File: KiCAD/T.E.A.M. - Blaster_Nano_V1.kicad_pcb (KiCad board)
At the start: 2 copper layers, 100.2 x 60 mm, 47 parts, among them J1 USB_C_Receptacle_USB2.0_14P, J2 Akku, J3 LED, J4 Taster, J5 Speaker, J6 Conn_02x03_Counter_Clockwise, Q1 FS8205A, U1 TP4056-42-ESOP8, U2 DW01A, U3 MT3608, U4 ATMEGA328P-AU, U5 CH340G, U6 DFR0299, Y1 Crystal_GND34, Y2 Crystal_GND34

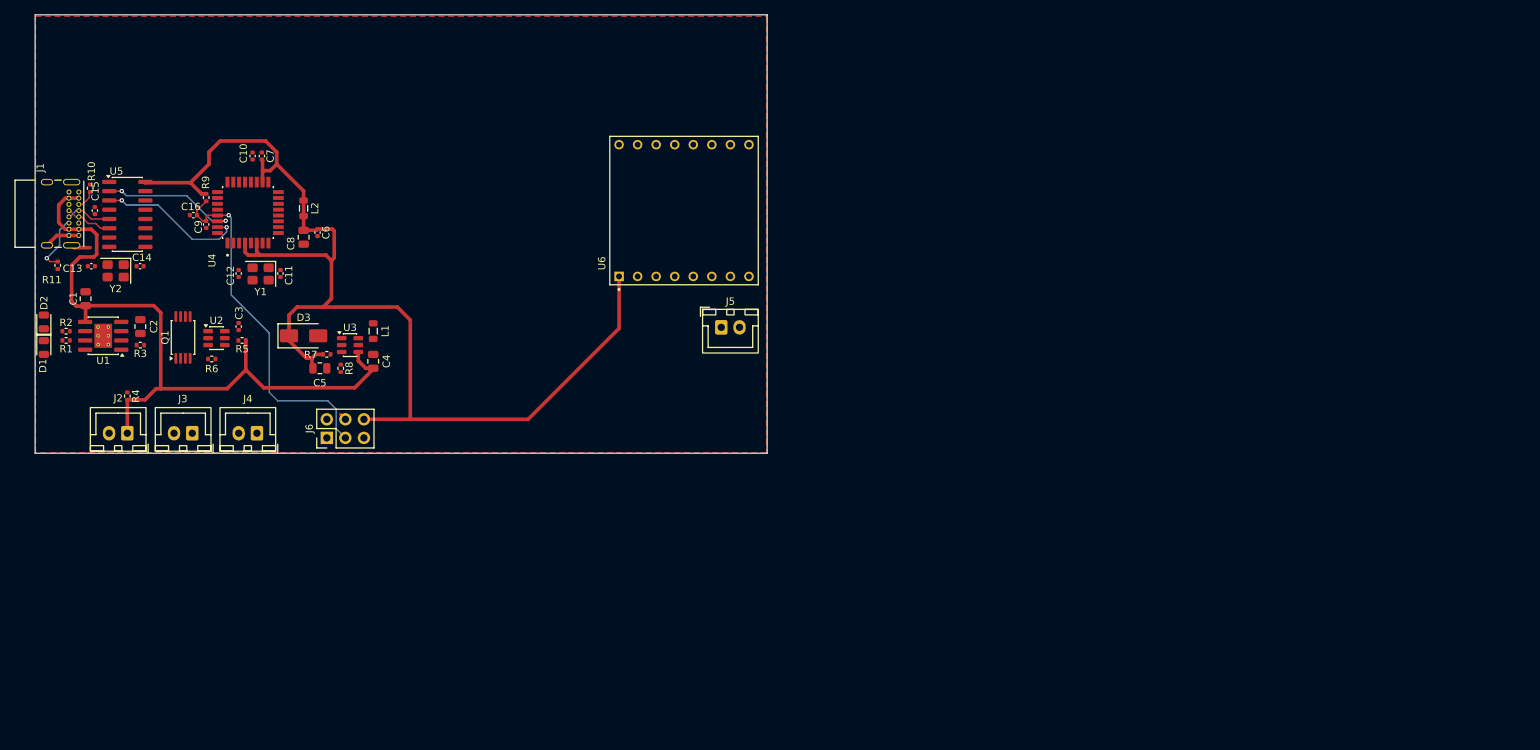
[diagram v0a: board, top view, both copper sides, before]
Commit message: Schaltplan finalisiert: alle Sektoren abgeschlossen
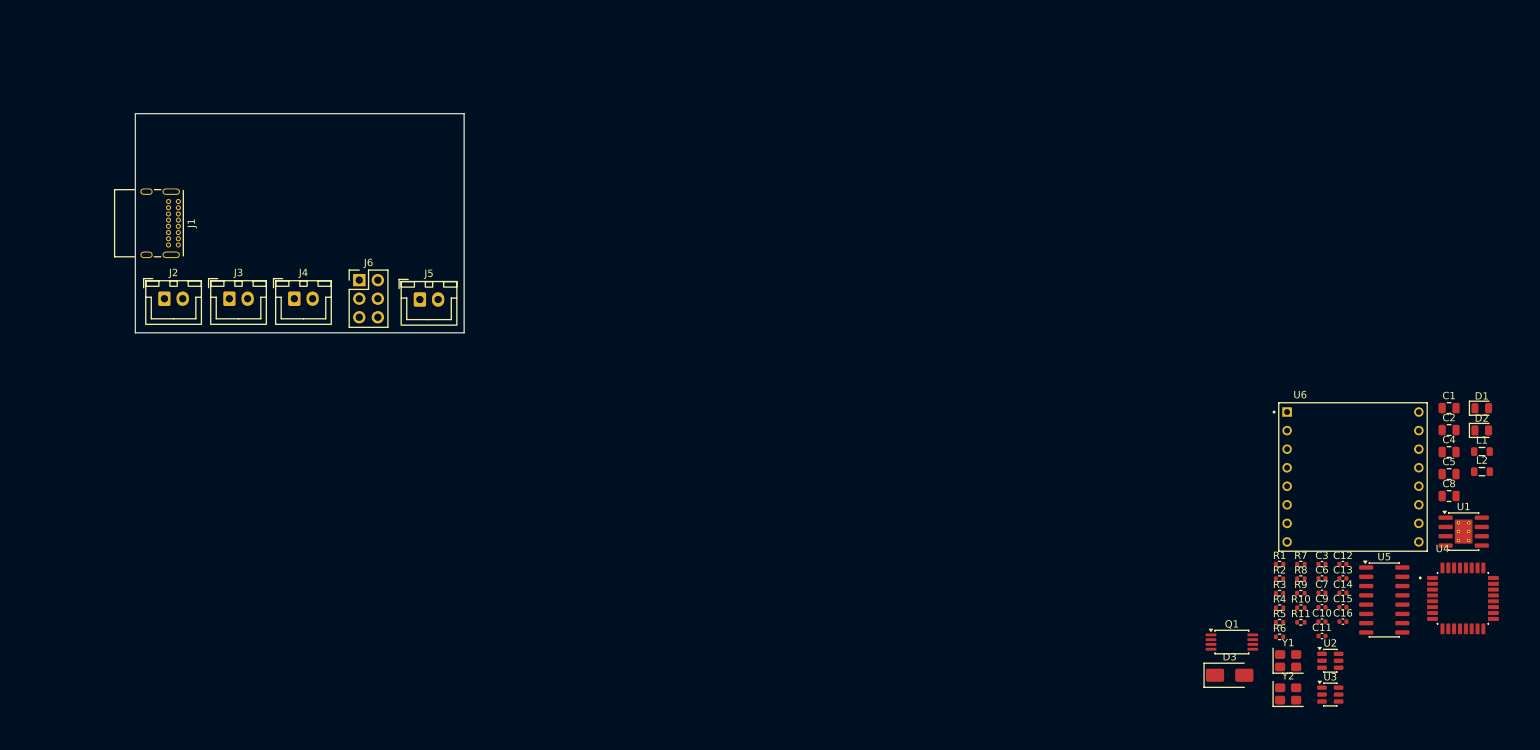
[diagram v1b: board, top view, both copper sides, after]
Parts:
- D1: value LED rot -> LED
- D2: value LED blau -> LED
- J6: value Conn_02x03_Counter_Clockwise -> ISP Bootloader
- moved D2 197.4 mm to (274.3, 118.4), turned to 0 degrees
- moved D1 197.0 mm to (274.3, 115.3), turned to 0 degrees
- moved U1 188.1 mm to (271.8, 132.2), turned to 0 degrees
- moved C1 187.2 mm to (269.8, 115.3), turned to 0 degrees
- moved U5 180.0 mm to (261.0, 141.6)
- moved C2 179.7 mm to (269.8, 118.3), turned to 0 degrees
- moved C15 179.3 mm to (255.3, 142.6), turned to 0 degrees
- moved R11 177.0 mm to (249.5, 144.6), turned to 0 degrees
- moved C13 176.6 mm to (255.3, 138.6)
- moved R10 175.4 mm to (249.5, 142.6), turned to 0 degrees
- moved U4 174.5 mm to (271.7, 141.3), turned to 0 degrees
- moved Y2 170.6 mm to (247.8, 154.4), turned to 0 degrees
- moved C14 170.6 mm to (255.3, 140.6), turned to 0 degrees
- moved R2 169.5 mm to (246.6, 138.7)
- moved R1 168.9 mm to (246.6, 136.7), turned to 0 degrees
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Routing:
- net VCC: track 162.8 -> 0.00 mm
- net VBATT: track 98.5 -> 0.00 mm
- net /RESET: track 48.9 -> 0.00 mm, vias 1 -> 0
- net /MCU_TX: track 20.6 -> 0.00 mm, vias 2 -> 0
- net /MCU_RX: track 18.8 -> 0.00 mm, vias 2 -> 0
- net GND: track 8.49 -> 0.00 mm
- net Net-(J1-CC2): track 8.25 -> 0.00 mm, vias 1 -> 0
- net /USB_DM: track 6.52 -> 0.00 mm
- net /USB_DP: track 6.34 -> 0.00 mm
- net Net-(J1-CC1): track 2.64 -> 0.00 mm
- removed copper zone on F.Cu, net GND
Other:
- board size 100.2 x 60 mm -> 45 x 30 mm

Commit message: Sektor 1: Placement und Routing abgeschlossen
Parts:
- removed C9: C, Capacitor_SMD:C_0402_1005Metric
- C1, C2, C8: value C -> 10 µF
- C10, C15, C16, C3, C6, C7: value C -> 100 nF
- C11, C12, C13, C14: value C -> 22 pF
- C4: value C -> 22µF
- C5: value C -> 22 µF
- D1: value LED -> LED rot
- D2: value LED -> LED blau
- J6: value ISP Bootloader -> Conn_02x03_Counter_Clockwise
- L1, L2: value L_Small -> 10 µH
- R1, R2: value R -> 1kΩ
- R10, R11: value R -> 5.1 kΩ
- R3: value R -> 2.4 kΩ
- R4: value R -> 470 Ω
- R5: value R -> 100 Ω
- R6: value R -> 1 kΩ
- R7: value R -> 180 kΩ
- R8: value R -> 27 kΩ
- R9: value R -> 10 kΩ
- Y1: value Crystal_GND34 -> 16 MHz
- Y2: value Crystal_GND34 -> 12 MHz
- moved U1 174.9 mm to (103.9, 83.2)
- moved C2 173.0 mm to (99.7, 87.0)
- moved D2 167.9 mm to (109.8, 84.5)
- moved D1 167.8 mm to (109.8, 81.9)
- moved C1 166.2 mm to (106.0, 87.0)
- moved R10 163.9 mm to (97.8, 80.6), turned to 90 degrees
- moved R11 162.3 mm to (99.1, 83.8)
- moved U2 161.9 mm to (102.3, 92.2), turned to 90 degrees
- moved R4 159.0 mm to (98.4, 85.1), turned to 180 degrees
- moved R3 158.3 mm to (99.7, 81.8), turned to -90 degrees
- moved C3 157.9 mm to (101.8, 89.5), turned to 180 degrees
- moved R5 154.6 mm to (102.9, 87.6), turned to -90 degrees
- moved R6 153.1 mm to (102.2, 95.8), turned to -90 degrees
- moved Q1 144.8 mm to (106.0, 92.7), turned to -90 degrees
- moved R1 144.6 mm to (112.8, 81.9)
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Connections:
- net Net-(J1-CC1) renamed /CC1
- net Net-(J1-CC2) renamed /CC2
- net Net-(U1-PROG) renamed /PROG
- net Net-(U2-CS) renamed /CS
- net Net-(U2-OC) renamed /OC
- net Net-(U2-OD) renamed /OD
- net Net-(U2-VCC) renamed /VCC_PROT
- C2 pad 2: Net-(D1-A) -> /VUSB
- C7 pad 2: VCC -> Net-(U4-AVCC)
- D1 pad 1: Net-(D1-K) -> /CHRG
- D1 pad 2: Net-(D1-A) -> /LED_CHRG
- D2 pad 1: Net-(D2-K) -> /STDBY
- D2 pad 2: Net-(D1-A) -> /LED_STDBY
- J1 pad A4: VBATT -> /VBUS
- J1 pad A9: VBATT -> /VBUS
- J1 pad B4: VBATT -> /VBUS
- J1 pad B9: VBATT -> /VBUS
- L2 pad 1: VCC -> Net-(U4-AVCC)
- R1 pad 1: Net-(U1-~{CHRG}) -> /LED_CHRG
- R1 pad 2: Net-(D1-K) -> /VUSB
- R2 pad 1: Net-(D2-K) -> /VUSB
- R2 pad 2: Net-(U1-~{STDBY}) -> /LED_STDBY
- R4 pad 1: Net-(D1-A) -> /VUSB
- R4 pad 2: VBATT -> /VBUS
- U1 pad 4: Net-(D1-A) -> /VUSB
- U1 pad 6: Net-(U1-~{STDBY}) -> /STDBY
- U1 pad 7: Net-(U1-~{CHRG}) -> /CHRG
- U1 pad 8: Net-(D1-A) -> /VUSB
- U4 pad 18: VCC -> Net-(U4-AVCC)
- U4 pad 9: /LED -> Net-(U4-PD5)
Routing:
- net GND: track 0.00 -> 47.5 mm
- net /VUSB: track 0.00 -> 30.8 mm, vias 0 -> 2
- net /CC2: track 0.00 -> 18.1 mm, vias 0 -> 2
- net VBATT: track 0.00 -> 15.7 mm
- net /VBUS: track 0.00 -> 10.9 mm
- net /OD: track 0.00 -> 6.89 mm
- net /OC: track 0.00 -> 3.82 mm
- net /VCC_PROT: track 0.00 -> 3.23 mm
- net /STDBY: track 0.00 -> 2.80 mm
- net /CHRG: track 0.00 -> 2.80 mm
- net /CC1: track 0.00 -> 2.00 mm
- net /CS: track 0.00 -> 1.94 mm
- net /PROG: track 0.00 -> 1.82 mm
- net /LED_STDBY: track 0.00 -> 1.55 mm
- net /LED_CHRG: track 0.00 -> 1.55 mm
